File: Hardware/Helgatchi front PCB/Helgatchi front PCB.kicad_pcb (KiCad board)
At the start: 2 copper layers, 156.1 x 80.3 mm, 45 parts, among them J3 SPI Screen, M1 MOTOR, Q1 NMOS, Q2 NMOS, SW1 SW_LEFT, SW2 SW_CENTER, SW3 SW_RIGHT, U1 XIAO-ESP32-S3

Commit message: R2
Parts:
- removed BZ1: BUZZER, Connector_PinHeader_2.54mm:PinHeader_1x02_P2.54mm_Vertical
- removed the G*** at (152.4, 81.9)
- removed the G*** at (135.9, 96.5)
- removed the G*** at (168.9, 96.5)
- removed the H1 at (189.2, 83.2)
- removed the H1 at (135.9, 82.5)
- removed the H2 at (168.9, 82.5)
- removed the H2 at (222.2, 83.2)
- removed H3 (x2), H4 (x2): M2, MountingHole:MountingHole_2.2mm_M2_Pad
- removed the J3 at (95.0, 84.0)
- removed the J3 at (152.4, 93.3)
- removed Q2: NMOS, Package_TO_SOT_SMD:SOT-23
- removed R2: 100kΩ, Resistor_SMD:R_0603_1608Metric
- removed the REF** at (95.0, 64.7)
- removed the REF** at (114.0, 134.0)
- removed the REF** at (76.0, 134.0)
- removed the REF** at (76.0, 66.0)
- removed the REF** at (114.0, 66.0)
- removed the REF** at (109.0, 124.0)
- removed the SW1 at (105.0, 104.0)
- removed the SW1 at (142.2, 110.5)
- removed the SW1 at (95.0, 107.0)
- removed the SW1 at (85.0, 104.0)
- removed the U1 at (152.4, 128.9)
- removed the U1 at (95.0, 127.5)
- removed the Untitled at (287.8, 115.7)
- added C3: 100nF, Capacitor_SMD:C_0603_1608Metric, B.Cu at (147.5, 78.5)
- added C7: 10uF, Capacitor_SMD:C_0603_1608Metric, B.Cu at (178.0, 124.8)
- added D4: WS2812C, WS2812B 2020:LED_WS2812B-2020_PLCC4_2.0x2.0mm, B.Cu at (147.5, 76.5)
- added G***: LOGO, LOGO, F.Cu at (164.0, 127.5)
- added G***: LOGO, LOGO, F.Cu at (113.5, 98.5)
- added H1: M2, Mounting_Wuerth:Mounting_Wuerth_WA-SMSI-M2_H8mm_9774080243, B.Cu at (183.0, 132.5)
- added H2: M2, Mounting_Wuerth:Mounting_Wuerth_WA-SMSI-M2_H8mm_9774080243, B.Cu at (129.7, 64.3)
- added H2: M2, Mounting_Wuerth:Mounting_Wuerth_WA-SMSI-M2_H8mm_9774080243, B.Cu at (129.7, 88.7)
- added H2: M2, Mounting_Wuerth:Mounting_Wuerth_WA-SMSI-M2_H8mm_9774080243, B.Cu at (97.9, 88.7)
- added H2: M2, Mounting_Wuerth:Mounting_Wuerth_WA-SMSI-M2_H8mm_9774080243, B.Cu at (145.0, 132.5)
- added H2: M2, Mounting_Wuerth:Mounting_Wuerth_WA-SMSI-M2_H8mm_9774080243, B.Cu at (97.9, 64.3)
- added J1: BATTERY, Connector_JST:JST_SH_SM02B-SRSS-TB_1x02-1MP_P1.00mm_Horizontal, B.Cu at (177.0, 115.5)
- added J2: SCREEN, Connector_Molex:Molex_PicoBlade_53261-0871_1x08-1MP_P1.25mm_Horizontal, B.Cu at (164.1, 94.6)
- added J3: SMA, Connector_Coaxial:SMA_Samtec_SMA-J-P-H-ST-EM1_EdgeMount, B.Cu at (113.8, 61.7)
- added J4: u.FL, Connector_Coaxial:U.FL_Molex_MCRF_73412-0110_Vertical, B.Cu at (99.3, 76.5)
- added JP1: LEDs, Jumper:SolderJumper-3_P1.3mm_Open_RoundedPad1.0x1.5mm_NumberLabels, B.Cu at (176.0, 124.0)
- added REF**: MountingHole_2.2mm_M2_Pad_Via, MountingHole:MountingHole_2.2mm_M2_Pad_Via, B.Cu at (132.8, 132.5)
- added REF**: MountingHole_2.2mm_M2_Pad_Via, MountingHole:MountingHole_2.2mm_M2_Pad_Via, B.Cu at (94.8, 132.5)
- added SW1: LEFT BUTTON, Reverse mount button:Reverse button footprint, B.Cu at (153.0, 102.5)
- added U1: XIAO ESP32-S3, Seeed Studio XIAO Series Footprints:XIAO-ESP32S3-SMD, B.Cu at (164.0, 126.5)
- added Untitled: Waveshare 1.69", 1.69 inch LCDs:Waveshare 1.69_, F.Cu at (164.0, 76.5)
- added kibuzzard-6976EA3A: G***, kibuzzard-6976EA3A, F.Cu at (175.0, 106.5)
- added kibuzzard-6976EA47: G***, kibuzzard-6976EA47, F.Cu at (153.0, 106.5)
- added kibuzzard-6976EA63: G***, kibuzzard-6976EA63, F.Cu at (164.0, 101.5)
- added kibuzzard-6976EDA9: G***, kibuzzard-6976EDA9, F.Cu at (166.0, 132.5)
- added kibuzzard-6976EEFC: G***, kibuzzard-6976EEFC, F.Cu at (164.0, 96.0)
- added kibuzzard-6976EF0C: G***, kibuzzard-6976EF0C, F.Cu at (164.0, 112.0)
- D1: footprint Diode_SMD:D_1206_3216Metric_Pad1.42x1.75mm_HandSolder -> Diode_SMD:D_0603_1608Metric
- D2, D3, D5, D6, D7: value WS2812B -> WS2812C; footprint LED_SMD:LED_WS2812B-2020_PLCC4_2.0x2.0mm -> WS2812B 2020:LED_WS2812B-2020_PLCC4_2.0x2.0mm
- SW2: value SW_CENTER -> CENTER BUTTON
- SW3: value SW_RIGHT -> RIGHT BUTTON
- moved D7 31.1 mm to (180.5, 121.5), turned to 0 degrees
- moved C6 29.9 mm to (180.5, 123.5), turned to 180 degrees
- moved C5 24.7 mm to (180.5, 100.5)
- moved D6 24.5 mm to (180.5, 98.5)
- moved D5 24.1 mm to (180.5, 76.5), turned to 0 degrees
- moved C4 21.3 mm to (180.5, 78.5), turned to 180 degrees
- moved SW3 14.8 mm to (175.0, 102.5), turned to 90 degrees
- moved M1 14.4 mm to (149.7, 117.0), turned to -90 degrees
- moved SW2 13.8 mm to (164.0, 105.5), turned to 90 degrees
- moved D1 13.0 mm to (152.0, 121.5), turned to 0 degrees
- moved Q1 12.9 mm to (151.6, 124.0), turned to 180 degrees
- moved C2 12.6 mm to (147.5, 100.5), turned to 180 degrees
- moved D3 9.90 mm to (147.5, 98.5), turned to 0 degrees
- moved R1 9.89 mm to (151.7, 126.5), turned to 180 degrees
- moved D2 8.17 mm to (147.5, 121.5)
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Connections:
- net +BATT renamed LED_PWR
- D5 pad 4: Net-(D3-DOUT) -> Net-(D4-DOUT)
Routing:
- net Net-(D4-DOUT): track 0.00 -> 51.4 mm
- net SPI_BL: track 0.00 -> 46.0 mm, vias 0 -> 2
- net LED_PWR: track 161.6 -> 195.9 mm, vias 10 -> 0
- net +BATT: track 0.00 -> 33.5 mm
- net (no net): track 0.00 -> 29.1 mm, vias 0 -> 12
- net +3.3V: track 60.3 -> 89.4 mm, vias 0 -> 3
- net Net-(D3-DOUT): track 50.1 -> 23.9 mm, vias 2 -> 0
- net -BATT: track 0.00 -> 25.5 mm, vias 10 -> 0
- net Net-(J3-In): track 0.00 -> 24.4 mm
- net BUTTON_CENTER: track 11.2 -> 24.4 mm, vias 2 -> 0
- net BUTTON_LEFT: track 12.9 -> 24.8 mm, vias 2 -> 0
- net BUTTON_RIGHT: track 23.3 -> 33.9 mm, vias 2 -> 0
- net SPI_RES: track 24.4 -> 34.3 mm, vias 1 -> 2
- net Net-(D6-DOUT): track 19.2 -> 26.4 mm
- net Net-(D5-DOUT): track 20.0 -> 27.0 mm, vias 2 -> 0
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- removed copper zone on B.Cu, net -BATT
- removed copper zone on F.Cu, net -BATT
- removed copper zone on B.Cu, net LED_PWR
- removed copper zone on F.Cu, net LED_PWR
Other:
- board size 156.1 x 80.3 mm -> 100.2 x 80 mm
- board text added: "+"
- board text added: "-"
- board text added: "2.4GHZ ANTENNA"
- board text added: "BL"
- board text added: "CLK"
- board text added: "CREDITS"
- board text added: "CS"
- board text added: "DC"
- board text added: "DIN"
- board text added: "GND"
- board text added: "Netkisune Poly801 kimb3r n1ghtbl00d Wade"
- board text added: "RST"
- board text added: "VCC"
- board text removed: "(BAAA)"
- board text removed: "+BATT"
- board text removed: "-BATT"
- board text removed: "<BAAA"
- board text removed: "BAAA>"
- board text removed: "HELGATCHI PROTOTYPE"
- board text removed: "Pips801"

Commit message: slopsoftware
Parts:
- removed the G*** at (113.5, 98.5)
- removed the H2 at (129.7, 64.3)
- removed the H2 at (129.7, 88.7)
- removed the H2 at (97.9, 88.7)
- removed the H2 at (97.9, 64.3)
- removed J3: SMA, Connector_Coaxial:SMA_Samtec_SMA-J-P-H-ST-EM1_EdgeMount
- removed J4: u.FL, Connector_Coaxial:U.FL_Molex_MCRF_73412-0110_Vertical
- removed REF** (x2): MountingHole_2.2mm_M2_Pad_Via, MountingHole:MountingHole_2.2mm_M2_Pad_Via
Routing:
- net Net-(J3-In): track 24.4 -> 0.00 mm
- net (no net): track 29.1 -> 14.5 mm, vias 12 -> 6
- net GND: vias 90 -> 15
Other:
- board size 100.2 x 80 mm -> 50 x 80 mm
- board text removed: "2.4GHZ ANTENNA"
- board text removed: "CREDITS"
- board text removed: "Netkisune Poly801 kimb3r n1ghtbl00d Wade"

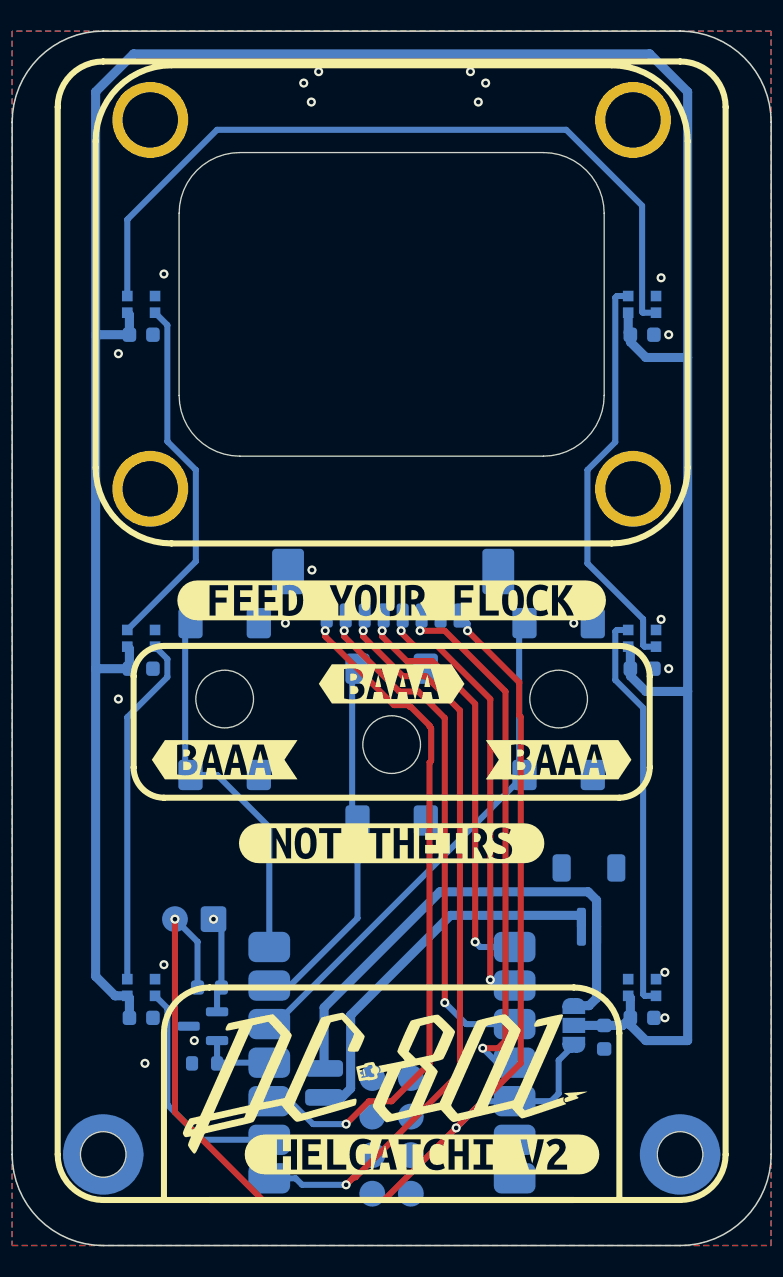
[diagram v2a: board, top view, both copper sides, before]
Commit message: Swap to WS2812B-4020-H2 Footprint variant
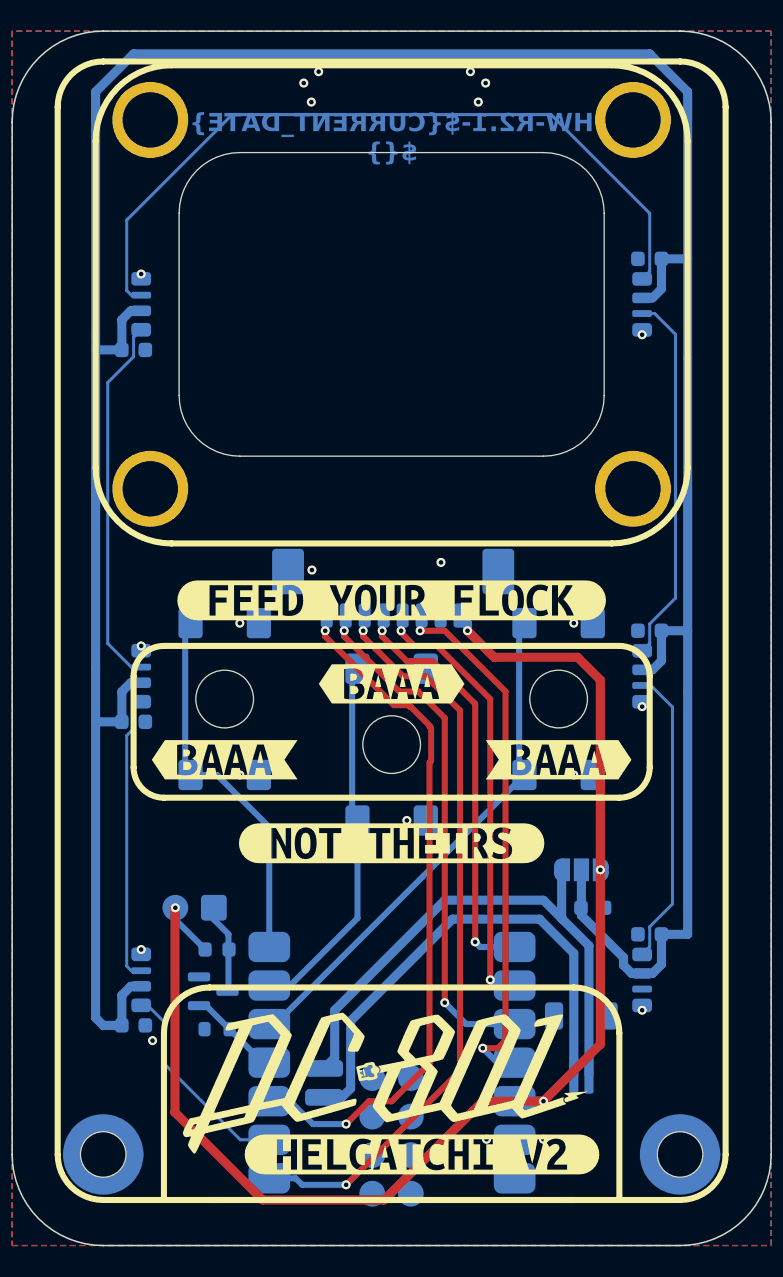
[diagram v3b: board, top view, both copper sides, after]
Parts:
- D2, D3, D4, D5, D6, D7: value WS2812C -> WS2812C-4020-H2; footprint WS2812B 2020:LED_WS2812B-2020_PLCC4_2.0x2.0mm -> WS2812:WS2812C-4020-H2
- moved JP1 10.3 mm to (176.5, 113.8), turned to 180 degrees
- moved J1 9.76 mm to (176.5, 125.2)
- moved C7 8.56 mm to (177.2, 116.2), turned to 0 degrees
- moved C6 5.52 mm to (181.0, 118.0), turned to 0 degrees
- moved C4 5.02 mm to (181.0, 73.5), turned to 0 degrees
- moved C2 3.54 mm to (147.0, 104.0)
- moved C5 2.55 mm to (181.0, 98.0), turned to 0 degrees
- moved D1 2.55 mm to (152.5, 119.0)
- moved D3 2.50 mm to (147.5, 101.0), turned to -90 degrees
- moved D6 2.50 mm to (180.5, 101.0), turned to 90 degrees
- moved Q1 2.40 mm to (152.2, 121.8), turned to 0 degrees
- moved R1 2.40 mm to (152.5, 124.2)
- moved C3 1.12 mm to (147.0, 79.5)
- moved M1 0.75 mm to (149.8, 116.2)
- moved C1 0.71 mm to (147.0, 124.0)
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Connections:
- D2 pad 1: LED_PWR -> LED_CONTROL
- D2 pad 2: Net-(D2-DOUT) -> LED_PWR
- D2 pad 3: GND -> Net-(D2-DOUT)
- D2 pad 4: LED_CONTROL -> GND
- D3 pad 1: LED_PWR -> Net-(D2-DOUT)
- D3 pad 2: Net-(D3-DOUT) -> LED_PWR
- D3 pad 3: GND -> Net-(D3-DOUT)
- D3 pad 4: Net-(D2-DOUT) -> GND
- D4 pad 1: LED_PWR -> Net-(D3-DOUT)
- D4 pad 2: Net-(D4-DOUT) -> LED_PWR
- D4 pad 3: GND -> Net-(D4-DOUT)
- D4 pad 4: Net-(D3-DOUT) -> GND
- D5 pad 1: LED_PWR -> Net-(D4-DOUT)
- D5 pad 2: Net-(D5-DOUT) -> LED_PWR
- D5 pad 3: GND -> Net-(D5-DOUT)
- D5 pad 4: Net-(D4-DOUT) -> GND
- D6 pad 1: LED_PWR -> Net-(D5-DOUT)
- D6 pad 2: Net-(D6-DOUT) -> LED_PWR
- D6 pad 3: GND -> Net-(D6-DOUT)
- D6 pad 4: Net-(D5-DOUT) -> GND
- D7 pad 1: LED_PWR -> Net-(D6-DOUT)
- D7 pad 2: unconnected-(D7-DOUT-Pad2) -> LED_PWR
- D7 pad 3: GND -> unconnected-(D7-DOUT-Pad3)
- D7 pad 4: Net-(D6-DOUT) -> GND
- Q1 pad 1: Net-(D1-A) -> VIBRATE
- Q1 pad 2: VIBRATE -> GND
- Q1 pad 3: GND -> Net-(D1-A)
- Untitled pad : (no net) -> GND
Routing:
- net -BATT: track 25.5 -> 32.9 mm
- net Net-(D6-DOUT): track 26.4 -> 19.7 mm
- net Net-(D2-DOUT): track 23.3 -> 18.9 mm
- net +BATT: track 33.5 -> 36.9 mm
- net Net-(D5-DOUT): track 27.0 -> 24.5 mm
- net LED_PWR: track 195.9 -> 198.0 mm
- net LED_CONTROL: track 15.2 -> 13.7 mm
- net VIBRATE: track 4.96 -> 6.18 mm
- net Net-(D4-DOUT): track 51.4 -> 50.3 mm
- net Net-(D3-DOUT): track 23.9 -> 24.4 mm
- net Net-(D1-A): track 6.44 -> 5.92 mm, vias 1 -> 0
- net +3.3V: track 89.4 -> 89.1 mm, vias 3 -> 4
- net GND: vias 15 -> 16
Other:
- board text added: "HW-${REVISION}-${CURRENT_DATE} ${}"
